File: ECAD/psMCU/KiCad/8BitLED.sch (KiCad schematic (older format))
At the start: 16 parts

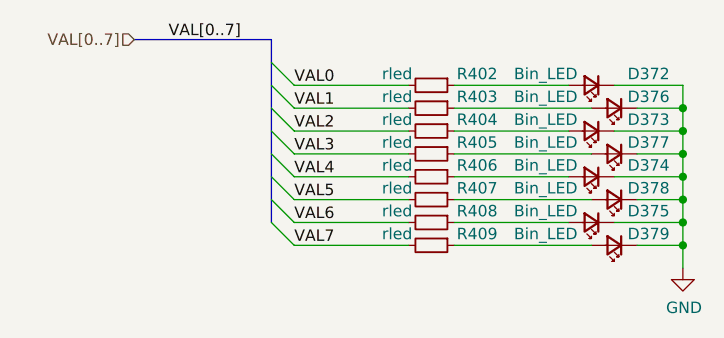
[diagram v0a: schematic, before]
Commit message: First draft v1.0 schematic done, ready for verify
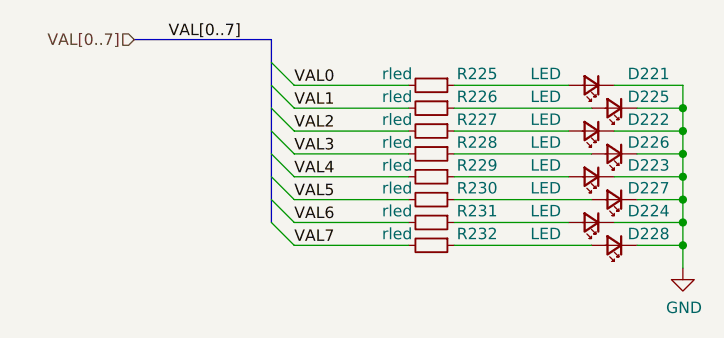
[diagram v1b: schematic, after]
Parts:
- D221, D222, D223, D224, D225, D226, D227, D228: value Bin_LED -> LED
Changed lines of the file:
@@
 $Descr A4 11693 8268
 encoding utf-8
-Sheet 78 93
+Sheet 45 98
 Title "psMCU"
 Date "2021-03-30"
-Rev "v0.1"
+Rev "v1.0"
 Comp "Philipp Schilk"
 Comment1 ""
@@
 AR Path="/61C3CF88/5F30EEBC/60378283" Ref="D338"  Part="1"
 AR Path="/5FF66C9F/604DCD27/60378283" Ref="D?"  Part="1"
-F 0 "D372" H 4700 2100 50  0000 C CNN
-F 1 "Bin_LED" H 5150 2100 50  0000 C CNN
+AR Path="/60E33DBC/609B0942/5F82FFCD/60378283" Ref="D?"  Part="1"
+F 0 "D221" H 4700 2100 50  0000 C CNN
+F 1 "LED" H 5150 2100 50  0000 C CNN
 F 2 "NoRef_Footprints:D_0603_1608Metric_NoRef" V 4950 2150 50  0001 C CNN
 F 3 "~" V 4950 2150 50  0001 C CNN
@@
 AR Path="/61C3CF88/5F30EEBC/60378284" Ref="D342"  Part="1"
 AR Path="/5FF66C9F/604DCD27/60378284" Ref="D?"  Part="1"
-F 0 "D376" H 4900 2200 50  0000 C CNN
-F 1 "Bin_LED" H 5350 2200 50  0000 C CNN
+AR Path="/60E33DBC/609B0942/5F82FFCD/60378284" Ref="D?"  Part="1"
+F 0 "D225" H 4900 2200 50  0000 C CNN
+F 1 "LED" H 5350 2200 50  0000 C CNN
 F 2 "NoRef_Footprints:D_0603_1608Metric_NoRef" V 5050 2250 50  0001 C CNN
 F 3 "~" V 5050 2250 50  0001 C CNN
@@
 AR Path="/61C3CF88/5F30EEBC/60378275" Ref="D339"  Part="1"
 AR Path="/5FF66C9F/604DCD27/60378275" Ref="D?"  Part="1"
-F 0 "D373" H 4700 2300 50  0000 C CNN
-F 1 "Bin_LED" H 5150 2300 50  0000 C CNN
+AR Path="/60E33DBC/609B0942/5F82FFCD/60378275" Ref="D?"  Part="1"
+F 0 "D222" H 4700 2300 50  0000 C CNN
+F 1 "LED" H 5150 2300 50  0000 C CNN
 F 2 "NoRef_Footprints:D_0603_1608Metric_NoRef" V 4950 2350 50  0001 C CNN
 F 3 "~" V 4950 2350 50  0001 C CNN
@@
 AR Path="/61C3CF88/5F30EEBC/5F5C55D2" Ref="D343"  Part="1"
 AR Path="/5FF66C9F/604DCD27/5F5C55D2" Ref="D?"  Part="1"
-F 0 "D377" H 4900 2400 50  0000 C CNN
-F 1 "Bin_LED" H 5350 2400 50  0000 C CNN
+AR Path="/60E33DBC/609B0942/5F82FFCD/5F5C55D2" Ref="D?"  Part="1"
+F 0 "D226" H 4900 2400 50  0000 C CNN
+F 1 "LED" H 5350 2400 50  0000 C CNN
 F 2 "NoRef_Footprints:D_0603_1608Metric_NoRef" V 5050 2450 50  0001 C CNN
 F 3 "~" V 5050 2450 50  0001 C CNN
@@
 AR Path="/61C3CF88/5F30EEBC/5F5C6722" Ref="D340"  Part="1"
 AR Path="/5FF66C9F/604DCD27/5F5C6722" Ref="D?"  Part="1"
-F 0 "D374" H 4700 2500 50  0000 C CNN
-F 1 "Bin_LED" H 5150 2500 50  0000 C CNN
+AR Path="/60E33DBC/609B0942/5F82FFCD/5F5C6722" Ref="D?"  Part="1"
+F 0 "D223" H 4700 2500 50  0000 C CNN
+F 1 "LED" H 5150 2500 50  0000 C CNN
 F 2 "NoRef_Footprints:D_0603_1608Metric_NoRef" V 4950 2550 50  0001 C CNN
 F 3 "~" V 4950 2550 50  0001 C CNN
@@
 AR Path="/61C3CF88/5F30EEBC/60378278" Ref="D344"  Part="1"
 AR Path="/5FF66C9F/604DCD27/60378278" Ref="D?"  Part="1"
-F 0 "D378" H 4900 2600 50  0000 C CNN
-F 1 "Bin_LED" H 5350 2600 50  0000 C CNN
+AR Path="/60E33DBC/609B0942/5F82FFCD/60378278" Ref="D?"  Part="1"
+F 0 "D227" H 4900 2600 50  0000 C CNN
+F 1 "LED" H 5350 2600 50  0000 C CNN
 F 2 "NoRef_Footprints:D_0603_1608Metric_NoRef" V 5050 2650 50  0001 C CNN
 F 3 "~" V 5050 2650 50  0001 C CNN
@@
 AR Path="/61C3CF88/5F30EEBC/60378279" Ref="D341"  Part="1"
 AR Path="/5FF66C9F/604DCD27/60378279" Ref="D?"  Part="1"
-F 0 "D375" H 4700 2700 50  0000 C CNN
-F 1 "Bin_LED" H 5150 2700 50  0000 C CNN
+AR Path="/60E33DBC/609B0942/5F82FFCD/60378279" Ref="D?"  Part="1"
+F 0 "D224" H 4700 2700 50  0000 C CNN
+F 1 "LED" H 5150 2700 50  0000 C CNN
 F 2 "NoRef_Footprints:D_0603_1608Metric_NoRef" V 4950 2750 50  0001 C CNN
 F 3 "~" V 4950 2750 50  0001 C CNN
@@
 AR Path="/61C3CF88/5F30EEBC/60527AB0" Ref="D345"  Part="1"
 AR Path="/5FF66C9F/604DCD27/60527AB0" Ref="D?"  Part="1"
-F 0 "D379" H 4900 2800 50  0000 C CNN
-F 1 "Bin_LED" H 5350 2800 50  0000 C CNN
+AR Path="/60E33DBC/609B0942/5F82FFCD/60527AB0" Ref="D?"  Part="1"
+F 0 "D228" H 4900 2800 50  0000 C CNN
+F 1 "LED" H 5350 2800 50  0000 C CNN
 F 2 "NoRef_Footprints:D_0603_1608Metric_NoRef" V 5050 2850 50  0001 C CNN
 F 3 "~" V 5050 2850 50  0001 C CNN
@@
 AR Path="/61C3CF88/5F30EEBC/60527ABA" Ref="#PWR01184"  Part="1"
 AR Path="/5FF66C9F/604DCD27/60527ABA" Ref="#PWR?"  Part="1"
-F 0 "#PWR01441" H 5350 2700 50  0001 C CNN
+AR Path="/60E33DBC/609B0942/5F82FFCD/60527ABA" Ref="#PWR?"  Part="1"
+F 0 "#PWR01023" H 5350 2700 50  0001 C CNN
 F 1 "GND" H 5355 2777 50  0000 C CNN
 F 2 "" H 5350 2950 50  0001 C CNN
@@
 AR Path="/60E33DBC/5F768DA1/5F82FFCD/665AE0E8" Ref="R257"  Part="1"
 AR Path="/5FF66C9F/604DCD27/665AE0E8" Ref="R?"  Part="1"
-F 0 "R402" V 4200 2350 50  0000 C CNN
+AR Path="/60E33DBC/609B0942/5F82FFCD/665AE0E8" Ref="R?"  Part="1"
+F 0 "R225" V 4200 2350 50  0000 C CNN
 F 1 "rled" V 4200 2000 50  0000 C CNN
 F 2 "NoRef_Footprints:R_0603_1608Metric_NoRef" H 4250 2150 50  0001 C CNN
@@
 AR Path="/60E33DBC/5F768DA1/5F82FFCD/665B3697" Ref="R258"  Part="1"
 AR Path="/5FF66C9F/604DCD27/665B3697" Ref="R?"  Part="1"
-F 0 "R403" V 4200 2450 50  0000 C CNN
+AR Path="/60E33DBC/609B0942/5F82FFCD/665B3697" Ref="R?"  Part="1"
+F 0 "R226" V 4200 2450 50  0000 C CNN
 F 1 "rled" V 4200 2100 50  0000 C CNN
 F 2 "NoRef_Footprints:R_0603_1608Metric_NoRef" H 4250 2250 50  0001 C CNN
@@
 AR Path="/60E33DBC/5F768DA1/5F82FFCD/665B39F4" Ref="R259"  Part="1"
 AR Path="/5FF66C9F/604DCD27/665B39F4" Ref="R?"  Part="1"
-F 0 "R404" V 4200 2550 50  0000 C CNN
+AR Path="/60E33DBC/609B0942/5F82FFCD/665B39F4" Ref="R?"  Part="1"
+F 0 "R227" V 4200 2550 50  0000 C CNN
 F 1 "rled" V 4200 2200 50  0000 C CNN
 F 2 "NoRef_Footprints:R_0603_1608Metric_NoRef" H 4250 2350 50  0001 C CNN
@@
 AR Path="/60E33DBC/5F768DA1/5F82FFCD/665B4197" Ref="R260"  Part="1"
 AR Path="/5FF66C9F/604DCD27/665B4197" Ref="R?"  Part="1"
-F 0 "R405" V 4200 2650 50  0000 C CNN
+AR Path="/60E33DBC/609B0942/5F82FFCD/665B4197" Ref="R?"  Part="1"
+F 0 "R228" V 4200 2650 50  0000 C CNN
 F 1 "rled" V 4200 2300 50  0000 C CNN
 F 2 "NoRef_Footprints:R_0603_1608Metric_NoRef" H 4250 2450 50  0001 C CNN
@@
 AR Path="/60E33DBC/5F768DA1/5F82FFCD/665B43F3" Ref="R261"  Part="1"
 AR Path="/5FF66C9F/604DCD27/665B43F3" Ref="R?"  Part="1"
-F 0 "R406" V 4200 2750 50  0000 C CNN
+AR Path="/60E33DBC/609B0942/5F82FFCD/665B43F3" Ref="R?"  Part="1"
+F 0 "R229" V 4200 2750 50  0000 C CNN
 F 1 "rled" V 4200 2400 50  0000 C CNN
 F 2 "NoRef_Footprints:R_0603_1608Metric_NoRef" H 4250 2550 50  0001 C CNN
@@
 AR Path="/60E33DBC/5F768DA1/5F82FFCD/665B4656" Ref="R262"  Part="1"
 AR Path="/5FF66C9F/604DCD27/665B4656" Ref="R?"  Part="1"
-F 0 "R407" V 4200 2850 50  0000 C CNN
+AR Path="/60E33DBC/609B0942/5F82FFCD/665B4656" Ref="R?"  Part="1"
+F 0 "R230" V 4200 2850 50  0000 C CNN
 F 1 "rled" V 4200 2500 50  0000 C CNN
 F 2 "NoRef_Footprints:R_0603_1608Metric_NoRef" H 4250 2650 50  0001 C CNN
@@
 AR Path="/60E33DBC/5F768DA1/5F82FFCD/665B49AB" Ref="R263"  Part="1"
 AR Path="/5FF66C9F/604DCD27/665B49AB" Ref="R?"  Part="1"
-F 0 "R408" V 4200 2950 50  0000 C CNN
+AR Path="/60E33DBC/609B0942/5F82FFCD/665B49AB" Ref="R?"  Part="1"
+F 0 "R231" V 4200 2950 50  0000 C CNN
 F 1 "rled" V 4200 2600 50  0000 C CNN
 F 2 "NoRef_Footprints:R_0603_1608Metric_NoRef" H 4250 2750 50  0001 C CNN
@@
 AR Path="/60E33DBC/5F768DA1/5F82FFCD/665B4D42" Ref="R264"  Part="1"
 AR Path="/5FF66C9F/604DCD27/665B4D42" Ref="R?"  Part="1"
-F 0 "R409" V 4200 3050 50  0000 C CNN
+AR Path="/60E33DBC/609B0942/5F82FFCD/665B4D42" Ref="R?"  Part="1"
+F 0 "R232" V 4200 3050 50  0000 C CNN
 F 1 "rled" V 4200 2700 50  0000 C CNN
 F 2 "NoRef_Footprints:R_0603_1608Metric_NoRef" H 4250 2850 50  0001 C CNN

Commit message: Annotation.
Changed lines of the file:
@@
 AR Path="/61C3CF88/5F30EEBC/60378283" Ref="D338"  Part="1"
 AR Path="/5FF66C9F/604DCD27/60378283" Ref="D?"  Part="1"
-AR Path="/60E33DBC/609B0942/5F82FFCD/60378283" Ref="D?"  Part="1"
-F 0 "D221" H 4700 2100 50  0000 C CNN
+AR Path="/60E33DBC/609B0942/5F82FFCD/60378283" Ref="D76"  Part="1"
+F 0 "D372" H 4700 2100 50  0000 C CNN
 F 1 "LED" H 5150 2100 50  0000 C CNN
 F 2 "NoRef_Footprints:D_0603_1608Metric_NoRef" V 4950 2150 50  0001 C CNN
@@
 AR Path="/61C3CF88/5F30EEBC/60378284" Ref="D342"  Part="1"
 AR Path="/5FF66C9F/604DCD27/60378284" Ref="D?"  Part="1"
-AR Path="/60E33DBC/609B0942/5F82FFCD/60378284" Ref="D?"  Part="1"
-F 0 "D225" H 4900 2200 50  0000 C CNN
+AR Path="/60E33DBC/609B0942/5F82FFCD/60378284" Ref="D80"  Part="1"
+F 0 "D376" H 4900 2200 50  0000 C CNN
 F 1 "LED" H 5350 2200 50  0000 C CNN
 F 2 "NoRef_Footprints:D_0603_1608Metric_NoRef" V 5050 2250 50  0001 C CNN
@@
 AR Path="/61C3CF88/5F30EEBC/60378275" Ref="D339"  Part="1"
 AR Path="/5FF66C9F/604DCD27/60378275" Ref="D?"  Part="1"
-AR Path="/60E33DBC/609B0942/5F82FFCD/60378275" Ref="D?"  Part="1"
-F 0 "D222" H 4700 2300 50  0000 C CNN
+AR Path="/60E33DBC/609B0942/5F82FFCD/60378275" Ref="D77"  Part="1"
+F 0 "D373" H 4700 2300 50  0000 C CNN
 F 1 "LED" H 5150 2300 50  0000 C CNN
 F 2 "NoRef_Footprints:D_0603_1608Metric_NoRef" V 4950 2350 50  0001 C CNN
@@
 AR Path="/61C3CF88/5F30EEBC/5F5C55D2" Ref="D343"  Part="1"
 AR Path="/5FF66C9F/604DCD27/5F5C55D2" Ref="D?"  Part="1"
-AR Path="/60E33DBC/609B0942/5F82FFCD/5F5C55D2" Ref="D?"  Part="1"
-F 0 "D226" H 4900 2400 50  0000 C CNN
+AR Path="/60E33DBC/609B0942/5F82FFCD/5F5C55D2" Ref="D81"  Part="1"
+F 0 "D377" H 4900 2400 50  0000 C CNN
 F 1 "LED" H 5350 2400 50  0000 C CNN
 F 2 "NoRef_Footprints:D_0603_1608Metric_NoRef" V 5050 2450 50  0001 C CNN
@@
 AR Path="/61C3CF88/5F30EEBC/5F5C6722" Ref="D340"  Part="1"
 AR Path="/5FF66C9F/604DCD27/5F5C6722" Ref="D?"  Part="1"
-AR Path="/60E33DBC/609B0942/5F82FFCD/5F5C6722" Ref="D?"  Part="1"
-F 0 "D223" H 4700 2500 50  0000 C CNN
+AR Path="/60E33DBC/609B0942/5F82FFCD/5F5C6722" Ref="D78"  Part="1"
+F 0 "D374" H 4700 2500 50  0000 C CNN
 F 1 "LED" H 5150 2500 50  0000 C CNN
 F 2 "NoRef_Footprints:D_0603_1608Metric_NoRef" V 4950 2550 50  0001 C CNN
@@
 AR Path="/61C3CF88/5F30EEBC/60378278" Ref="D344"  Part="1"
 AR Path="/5FF66C9F/604DCD27/60378278" Ref="D?"  Part="1"
-AR Path="/60E33DBC/609B0942/5F82FFCD/60378278" Ref="D?"  Part="1"
-F 0 "D227" H 4900 2600 50  0000 C CNN
+AR Path="/60E33DBC/609B0942/5F82FFCD/60378278" Ref="D82"  Part="1"
+F 0 "D378" H 4900 2600 50  0000 C CNN
 F 1 "LED" H 5350 2600 50  0000 C CNN
 F 2 "NoRef_Footprints:D_0603_1608Metric_NoRef" V 5050 2650 50  0001 C CNN
@@
 AR Path="/61C3CF88/5F30EEBC/60378279" Ref="D341"  Part="1"
 AR Path="/5FF66C9F/604DCD27/60378279" Ref="D?"  Part="1"
-AR Path="/60E33DBC/609B0942/5F82FFCD/60378279" Ref="D?"  Part="1"
-F 0 "D224" H 4700 2700 50  0000 C CNN
+AR Path="/60E33DBC/609B0942/5F82FFCD/60378279" Ref="D79"  Part="1"
+F 0 "D375" H 4700 2700 50  0000 C CNN
 F 1 "LED" H 5150 2700 50  0000 C CNN
 F 2 "NoRef_Footprints:D_0603_1608Metric_NoRef" V 4950 2750 50  0001 C CNN
@@
 AR Path="/61C3CF88/5F30EEBC/60527AB0" Ref="D345"  Part="1"
 AR Path="/5FF66C9F/604DCD27/60527AB0" Ref="D?"  Part="1"
-AR Path="/60E33DBC/609B0942/5F82FFCD/60527AB0" Ref="D?"  Part="1"
-F 0 "D228" H 4900 2800 50  0000 C CNN
+AR Path="/60E33DBC/609B0942/5F82FFCD/60527AB0" Ref="D83"  Part="1"
+F 0 "D379" H 4900 2800 50  0000 C CNN
 F 1 "LED" H 5350 2800 50  0000 C CNN
 F 2 "NoRef_Footprints:D_0603_1608Metric_NoRef" V 5050 2850 50  0001 C CNN
@@
 AR Path="/61C3CF88/5F30EEBC/60527ABA" Ref="#PWR01184"  Part="1"
 AR Path="/5FF66C9F/604DCD27/60527ABA" Ref="#PWR?"  Part="1"
-AR Path="/60E33DBC/609B0942/5F82FFCD/60527ABA" Ref="#PWR?"  Part="1"
-F 0 "#PWR01023" H 5350 2700 50  0001 C CNN
+AR Path="/60E33DBC/609B0942/5F82FFCD/60527ABA" Ref="#PWR0488"  Part="1"
+F 0 "#PWR01441" H 5350 2700 50  0001 C CNN
 F 1 "GND" H 5355 2777 50  0000 C CNN
 F 2 "" H 5350 2950 50  0001 C CNN
@@
 AR Path="/60E33DBC/5F768DA1/5F82FFCD/665AE0E8" Ref="R257"  Part="1"
 AR Path="/5FF66C9F/604DCD27/665AE0E8" Ref="R?"  Part="1"
-AR Path="/60E33DBC/609B0942/5F82FFCD/665AE0E8" Ref="R?"  Part="1"
-F 0 "R225" V 4200 2350 50  0000 C CNN
+AR Path="/60E33DBC/609B0942/5F82FFCD/665AE0E8" Ref="R84"  Part="1"
+F 0 "R402" V 4200 2350 50  0000 C CNN
 F 1 "rled" V 4200 2000 50  0000 C CNN
 F 2 "NoRef_Footprints:R_0603_1608Metric_NoRef" H 4250 2150 50  0001 C CNN
@@
 AR Path="/60E33DBC/5F768DA1/5F82FFCD/665B3697" Ref="R258"  Part="1"
 AR Path="/5FF66C9F/604DCD27/665B3697" Ref="R?"  Part="1"
-AR Path="/60E33DBC/609B0942/5F82FFCD/665B3697" Ref="R?"  Part="1"
-F 0 "R226" V 4200 2450 50  0000 C CNN
+AR Path="/60E33DBC/609B0942/5F82FFCD/665B3697" Ref="R85"  Part="1"
+F 0 "R403" V 4200 2450 50  0000 C CNN
 F 1 "rled" V 4200 2100 50  0000 C CNN
 F 2 "NoRef_Footprints:R_0603_1608Metric_NoRef" H 4250 2250 50  0001 C CNN
@@
 AR Path="/60E33DBC/5F768DA1/5F82FFCD/665B39F4" Ref="R259"  Part="1"
 AR Path="/5FF66C9F/604DCD27/665B39F4" Ref="R?"  Part="1"
-AR Path="/60E33DBC/609B0942/5F82FFCD/665B39F4" Ref="R?"  Part="1"
-F 0 "R227" V 4200 2550 50  0000 C CNN
+AR Path="/60E33DBC/609B0942/5F82FFCD/665B39F4" Ref="R86"  Part="1"
+F 0 "R404" V 4200 2550 50  0000 C CNN
 F 1 "rled" V 4200 2200 50  0000 C CNN
 F 2 "NoRef_Footprints:R_0603_1608Metric_NoRef" H 4250 2350 50  0001 C CNN
@@
 AR Path="/60E33DBC/5F768DA1/5F82FFCD/665B4197" Ref="R260"  Part="1"
 AR Path="/5FF66C9F/604DCD27/665B4197" Ref="R?"  Part="1"
-AR Path="/60E33DBC/609B0942/5F82FFCD/665B4197" Ref="R?"  Part="1"
-F 0 "R228" V 4200 2650 50  0000 C CNN
+AR Path="/60E33DBC/609B0942/5F82FFCD/665B4197" Ref="R87"  Part="1"
+F 0 "R405" V 4200 2650 50  0000 C CNN
 F 1 "rled" V 4200 2300 50  0000 C CNN
 F 2 "NoRef_Footprints:R_0603_1608Metric_NoRef" H 4250 2450 50  0001 C CNN
@@
 AR Path="/60E33DBC/5F768DA1/5F82FFCD/665B43F3" Ref="R261"  Part="1"
 AR Path="/5FF66C9F/604DCD27/665B43F3" Ref="R?"  Part="1"
-AR Path="/60E33DBC/609B0942/5F82FFCD/665B43F3" Ref="R?"  Part="1"
-F 0 "R229" V 4200 2750 50  0000 C CNN
+AR Path="/60E33DBC/609B0942/5F82FFCD/665B43F3" Ref="R88"  Part="1"
+F 0 "R406" V 4200 2750 50  0000 C CNN
 F 1 "rled" V 4200 2400 50  0000 C CNN
 F 2 "NoRef_Footprints:R_0603_1608Metric_NoRef" H 4250 2550 50  0001 C CNN
@@
 AR Path="/60E33DBC/5F768DA1/5F82FFCD/665B4656" Ref="R262"  Part="1"
 AR Path="/5FF66C9F/604DCD27/665B4656" Ref="R?"  Part="1"
-AR Path="/60E33DBC/609B0942/5F82FFCD/665B4656" Ref="R?"  Part="1"
-F 0 "R230" V 4200 2850 50  0000 C CNN
+AR Path="/60E33DBC/609B0942/5F82FFCD/665B4656" Ref="R89"  Part="1"
+F 0 "R407" V 4200 2850 50  0000 C CNN
 F 1 "rled" V 4200 2500 50  0000 C CNN
 F 2 "NoRef_Footprints:R_0603_1608Metric_NoRef" H 4250 2650 50  0001 C CNN
@@
 AR Path="/60E33DBC/5F768DA1/5F82FFCD/665B49AB" Ref="R263"  Part="1"
 AR Path="/5FF66C9F/604DCD27/665B49AB" Ref="R?"  Part="1"
-AR Path="/60E33DBC/609B0942/5F82FFCD/665B49AB" Ref="R?"  Part="1"
-F 0 "R231" V 4200 2950 50  0000 C CNN
+AR Path="/60E33DBC/609B0942/5F82FFCD/665B49AB" Ref="R90"  Part="1"
+F 0 "R408" V 4200 2950 50  0000 C CNN
 F 1 "rled" V 4200 2600 50  0000 C CNN
 F 2 "NoRef_Footprints:R_0603_1608Metric_NoRef" H 4250 2750 50  0001 C CNN
@@
 AR Path="/60E33DBC/5F768DA1/5F82FFCD/665B4D42" Ref="R264"  Part="1"
 AR Path="/5FF66C9F/604DCD27/665B4D42" Ref="R?"  Part="1"
-AR Path="/60E33DBC/609B0942/5F82FFCD/665B4D42" Ref="R?"  Part="1"
-F 0 "R232" V 4200 3050 50  0000 C CNN
+AR Path="/60E33DBC/609B0942/5F82FFCD/665B4D42" Ref="R91"  Part="1"
+F 0 "R409" V 4200 3050 50  0000 C CNN
 F 1 "rled" V 4200 2700 50  0000 C CNN
 F 2 "NoRef_Footprints:R_0603_1608Metric_NoRef" H 4250 2850 50  0001 C CNN

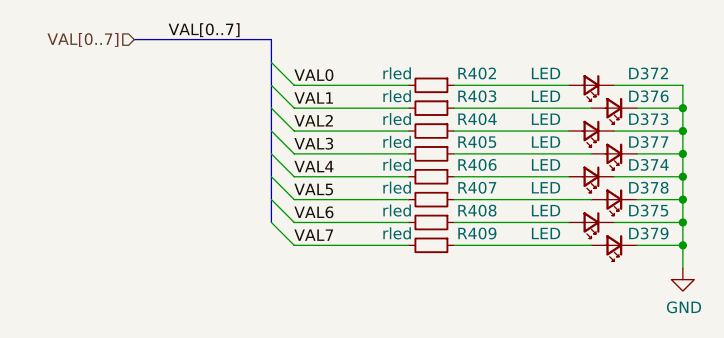
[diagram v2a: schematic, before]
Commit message: Updated Page Descriptions
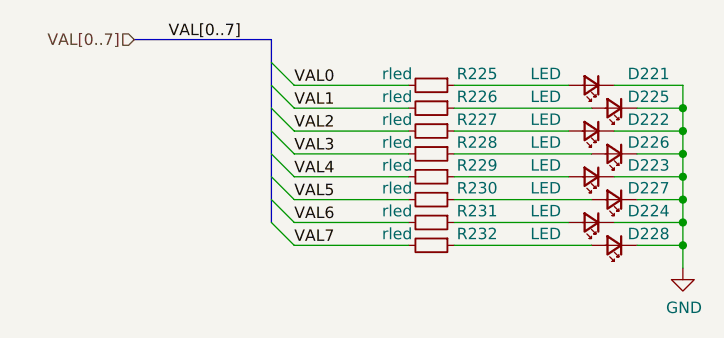
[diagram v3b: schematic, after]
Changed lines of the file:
@@
 $Descr A4 11693 8268
 encoding utf-8
-Sheet 45 98
+Sheet 6 98
 Title "psMCU"
 Date "2021-03-30"
@@
 AR Path="/5FF66C9F/604DCD27/60378283" Ref="D?"  Part="1"
 AR Path="/60E33DBC/609B0942/5F82FFCD/60378283" Ref="D76"  Part="1"
-F 0 "D372" H 4700 2100 50  0000 C CNN
+F 0 "D221" H 4700 2100 50  0000 C CNN
 F 1 "LED" H 5150 2100 50  0000 C CNN
 F 2 "NoRef_Footprints:D_0603_1608Metric_NoRef" V 4950 2150 50  0001 C CNN
@@
 AR Path="/5FF66C9F/604DCD27/60378284" Ref="D?"  Part="1"
 AR Path="/60E33DBC/609B0942/5F82FFCD/60378284" Ref="D80"  Part="1"
-F 0 "D376" H 4900 2200 50  0000 C CNN
+F 0 "D225" H 4900 2200 50  0000 C CNN
 F 1 "LED" H 5350 2200 50  0000 C CNN
 F 2 "NoRef_Footprints:D_0603_1608Metric_NoRef" V 5050 2250 50  0001 C CNN
@@
 AR Path="/5FF66C9F/604DCD27/60378275" Ref="D?"  Part="1"
 AR Path="/60E33DBC/609B0942/5F82FFCD/60378275" Ref="D77"  Part="1"
-F 0 "D373" H 4700 2300 50  0000 C CNN
+F 0 "D222" H 4700 2300 50  0000 C CNN
 F 1 "LED" H 5150 2300 50  0000 C CNN
 F 2 "NoRef_Footprints:D_0603_1608Metric_NoRef" V 4950 2350 50  0001 C CNN
@@
 AR Path="/5FF66C9F/604DCD27/5F5C55D2" Ref="D?"  Part="1"
 AR Path="/60E33DBC/609B0942/5F82FFCD/5F5C55D2" Ref="D81"  Part="1"
-F 0 "D377" H 4900 2400 50  0000 C CNN
+F 0 "D226" H 4900 2400 50  0000 C CNN
 F 1 "LED" H 5350 2400 50  0000 C CNN
 F 2 "NoRef_Footprints:D_0603_1608Metric_NoRef" V 5050 2450 50  0001 C CNN
@@
 AR Path="/5FF66C9F/604DCD27/5F5C6722" Ref="D?"  Part="1"
 AR Path="/60E33DBC/609B0942/5F82FFCD/5F5C6722" Ref="D78"  Part="1"
-F 0 "D374" H 4700 2500 50  0000 C CNN
+F 0 "D223" H 4700 2500 50  0000 C CNN
 F 1 "LED" H 5150 2500 50  0000 C CNN
 F 2 "NoRef_Footprints:D_0603_1608Metric_NoRef" V 4950 2550 50  0001 C CNN
@@
 AR Path="/5FF66C9F/604DCD27/60378278" Ref="D?"  Part="1"
 AR Path="/60E33DBC/609B0942/5F82FFCD/60378278" Ref="D82"  Part="1"
-F 0 "D378" H 4900 2600 50  0000 C CNN
+F 0 "D227" H 4900 2600 50  0000 C CNN
 F 1 "LED" H 5350 2600 50  0000 C CNN
 F 2 "NoRef_Footprints:D_0603_1608Metric_NoRef" V 5050 2650 50  0001 C CNN
@@
 AR Path="/5FF66C9F/604DCD27/60378279" Ref="D?"  Part="1"
 AR Path="/60E33DBC/609B0942/5F82FFCD/60378279" Ref="D79"  Part="1"
-F 0 "D375" H 4700 2700 50  0000 C CNN
+F 0 "D224" H 4700 2700 50  0000 C CNN
 F 1 "LED" H 5150 2700 50  0000 C CNN
 F 2 "NoRef_Footprints:D_0603_1608Metric_NoRef" V 4950 2750 50  0001 C CNN
@@
 AR Path="/5FF66C9F/604DCD27/60527AB0" Ref="D?"  Part="1"
 AR Path="/60E33DBC/609B0942/5F82FFCD/60527AB0" Ref="D83"  Part="1"
-F 0 "D379" H 4900 2800 50  0000 C CNN
+F 0 "D228" H 4900 2800 50  0000 C CNN
 F 1 "LED" H 5350 2800 50  0000 C CNN
 F 2 "NoRef_Footprints:D_0603_1608Metric_NoRef" V 5050 2850 50  0001 C CNN
@@
 AR Path="/5FF66C9F/604DCD27/60527ABA" Ref="#PWR?"  Part="1"
 AR Path="/60E33DBC/609B0942/5F82FFCD/60527ABA" Ref="#PWR0488"  Part="1"
-F 0 "#PWR01441" H 5350 2700 50  0001 C CNN
+F 0 "#PWR01023" H 5350 2700 50  0001 C CNN
 F 1 "GND" H 5355 2777 50  0000 C CNN
 F 2 "" H 5350 2950 50  0001 C CNN
@@
 AR Path="/5FF66C9F/604DCD27/665AE0E8" Ref="R?"  Part="1"
 AR Path="/60E33DBC/609B0942/5F82FFCD/665AE0E8" Ref="R84"  Part="1"
-F 0 "R402" V 4200 2350 50  0000 C CNN
+F 0 "R225" V 4200 2350 50  0000 C CNN
 F 1 "rled" V 4200 2000 50  0000 C CNN
 F 2 "NoRef_Footprints:R_0603_1608Metric_NoRef" H 4250 2150 50  0001 C CNN
@@
 AR Path="/5FF66C9F/604DCD27/665B3697" Ref="R?"  Part="1"
 AR Path="/60E33DBC/609B0942/5F82FFCD/665B3697" Ref="R85"  Part="1"
-F 0 "R403" V 4200 2450 50  0000 C CNN
+F 0 "R226" V 4200 2450 50  0000 C CNN
 F 1 "rled" V 4200 2100 50  0000 C CNN
 F 2 "NoRef_Footprints:R_0603_1608Metric_NoRef" H 4250 2250 50  0001 C CNN
@@
 AR Path="/5FF66C9F/604DCD27/665B39F4" Ref="R?"  Part="1"
 AR Path="/60E33DBC/609B0942/5F82FFCD/665B39F4" Ref="R86"  Part="1"
-F 0 "R404" V 4200 2550 50  0000 C CNN
+F 0 "R227" V 4200 2550 50  0000 C CNN
 F 1 "rled" V 4200 2200 50  0000 C CNN
 F 2 "NoRef_Footprints:R_0603_1608Metric_NoRef" H 4250 2350 50  0001 C CNN
@@
 AR Path="/5FF66C9F/604DCD27/665B4197" Ref="R?"  Part="1"
 AR Path="/60E33DBC/609B0942/5F82FFCD/665B4197" Ref="R87"  Part="1"
-F 0 "R405" V 4200 2650 50  0000 C CNN
+F 0 "R228" V 4200 2650 50  0000 C CNN
 F 1 "rled" V 4200 2300 50  0000 C CNN
 F 2 "NoRef_Footprints:R_0603_1608Metric_NoRef" H 4250 2450 50  0001 C CNN
@@
 AR Path="/5FF66C9F/604DCD27/665B43F3" Ref="R?"  Part="1"
 AR Path="/60E33DBC/609B0942/5F82FFCD/665B43F3" Ref="R88"  Part="1"
-F 0 "R406" V 4200 2750 50  0000 C CNN
+F 0 "R229" V 4200 2750 50  0000 C CNN
 F 1 "rled" V 4200 2400 50  0000 C CNN
 F 2 "NoRef_Footprints:R_0603_1608Metric_NoRef" H 4250 2550 50  0001 C CNN
@@
 AR Path="/5FF66C9F/604DCD27/665B4656" Ref="R?"  Part="1"
 AR Path="/60E33DBC/609B0942/5F82FFCD/665B4656" Ref="R89"  Part="1"
-F 0 "R407" V 4200 2850 50  0000 C CNN
+F 0 "R230" V 4200 2850 50  0000 C CNN
 F 1 "rled" V 4200 2500 50  0000 C CNN
 F 2 "NoRef_Footprints:R_0603_1608Metric_NoRef" H 4250 2650 50  0001 C CNN
@@
 AR Path="/5FF66C9F/604DCD27/665B49AB" Ref="R?"  Part="1"
 AR Path="/60E33DBC/609B0942/5F82FFCD/665B49AB" Ref="R90"  Part="1"
-F 0 "R408" V 4200 2950 50  0000 C CNN
+F 0 "R231" V 4200 2950 50  0000 C CNN
 F 1 "rled" V 4200 2600 50  0000 C CNN
 F 2 "NoRef_Footprints:R_0603_1608Metric_NoRef" H 4250 2750 50  0001 C CNN
@@
 AR Path="/5FF66C9F/604DCD27/665B4D42" Ref="R?"  Part="1"
 AR Path="/60E33DBC/609B0942/5F82FFCD/665B4D42" Ref="R91"  Part="1"
-F 0 "R409" V 4200 3050 50  0000 C CNN
+F 0 "R232" V 4200 3050 50  0000 C CNN
 F 1 "rled" V 4200 2700 50  0000 C CNN
 F 2 "NoRef_Footprints:R_0603_1608Metric_NoRef" H 4250 2850 50  0001 C CNN
